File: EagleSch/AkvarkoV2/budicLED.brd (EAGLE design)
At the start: 114.3 x 160 mm, 75 parts, among them IC1 7805T, IC2 4051N, IC3 LF33CV, IC4 ESP01, J1 TRANSFLASH-LOCK, Q1 BD243C, Q2 BD243C, Q3 BD243C, Q4 BD243C, T1 2N5551, T2 2N5551, T3 2N5551, T4 2N5551, U1 ARDUINOR3-DIMENSION, X1 SMKDSP_1,5/2, X2 SMKDSP_1,5/8, X3 SMKDSP_1,5/3

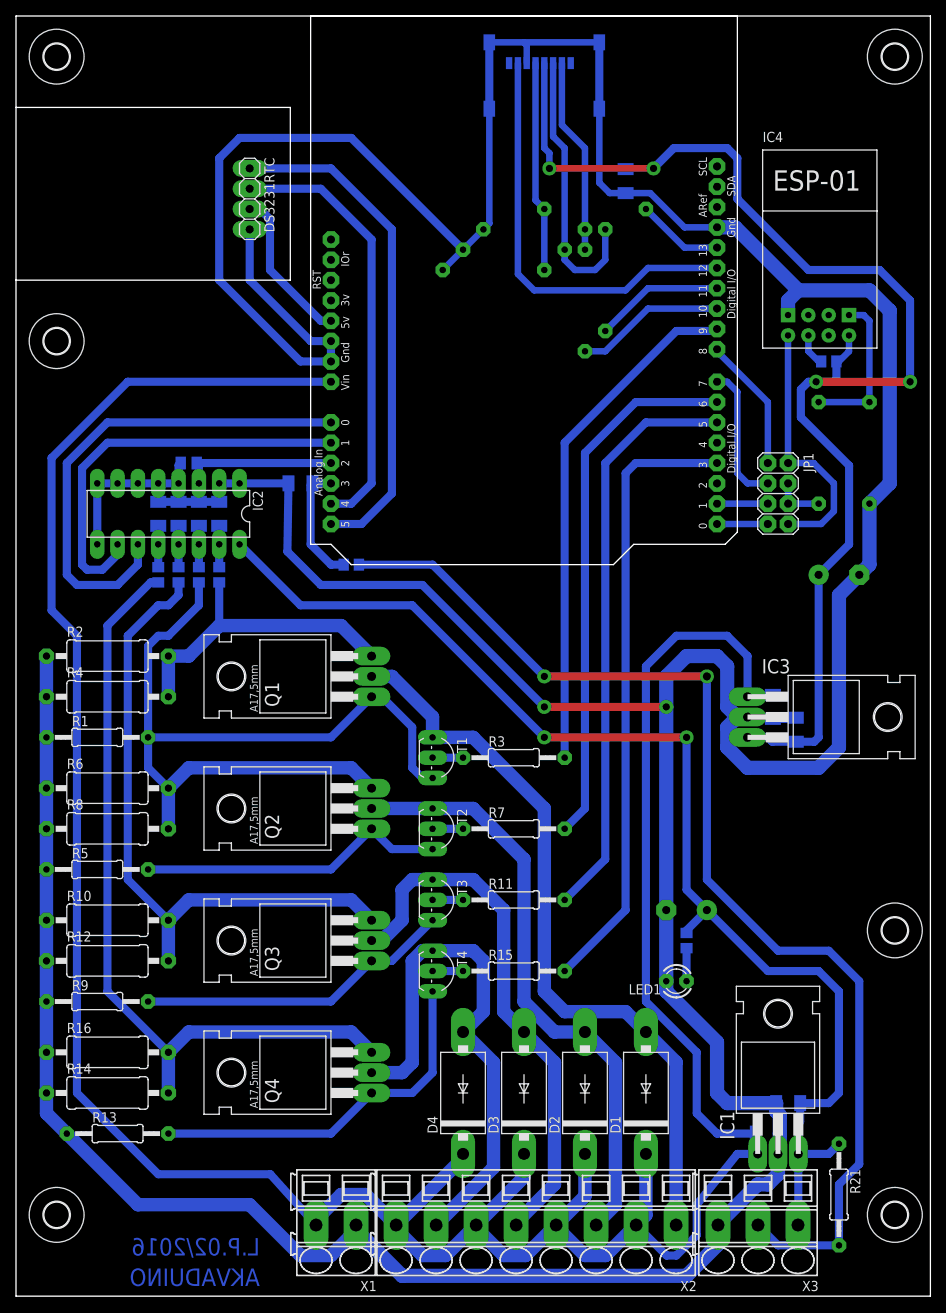
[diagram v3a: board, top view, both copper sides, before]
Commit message: DPS: - pridany LED, - dratove propojky nahrazeny reszistory 0R0, - doplnena rozlita med, - pridan zesilovaci prvek (tranzistor) k AD prevodnikum od snimani proudu ve vykonovem obvodu, - pridano nekolik filtracnich kapacit u napajeni IO.
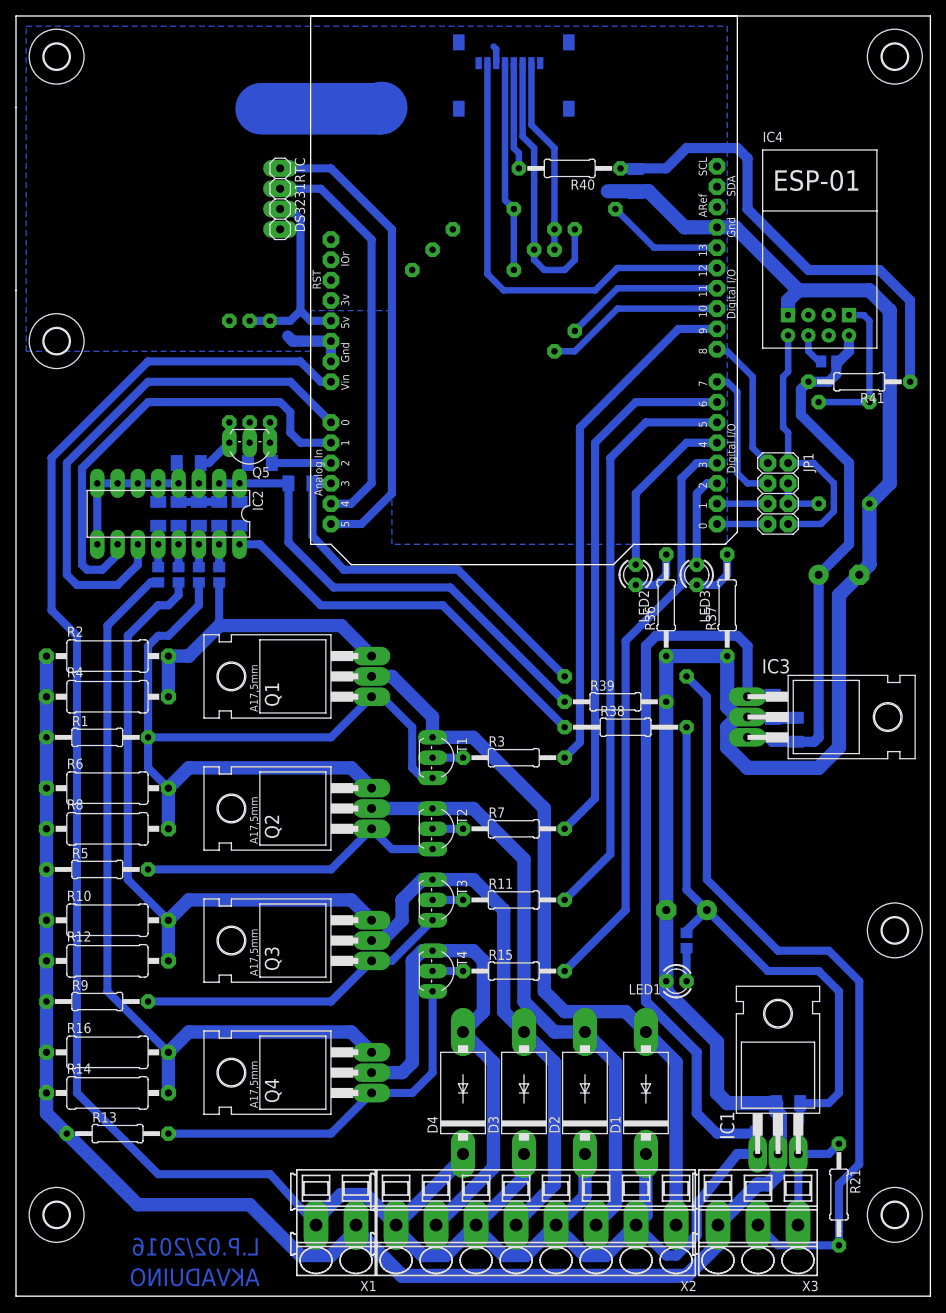
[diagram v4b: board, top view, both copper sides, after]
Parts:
- added C14, C15: 330n, rcl:C1206K
- added LED2, LED3: 2.2V 25mA, led:LED3MM
- added Q5: BC546A, transistor-npn:TO92-EBC
- added R33, R34, R35: 10k, rcl:0207/12
- added R36, R37: 390R, rcl:0207/12
- added R38: 0R0, rcl:0207/15
- added R39, R40, R41: 0R0, rcl:0207/12
- C11: device rcl:C0805K -> rcl:C1206K
- R17, R18, R19, R20: value 4k7 -> 1k
- R24: device rcl:R0805 -> rcl:0207/15
- moved R24 37.0 mm to (76.2, 77.5)
- moved J1 3.81 mm to (62.2, 153.7)
- moved DS3231RTC 3.81 mm to (33.0, 137.2)
- moved R25 3.81 mm to (68.6, 135.9)
- moved R27 3.81 mm to (69.8, 127.0)
- moved R29 3.81 mm to (67.3, 124.5)
- moved R26 3.81 mm to (55.9, 128.3)
- moved R28 3.81 mm to (58.4, 130.8)
- moved R30 3.81 mm to (61.0, 133.3)
- moved C13 1.27 mm to (77.5, 139.4)
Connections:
- new net GNDA: C1.2, C11.2, C12.2, C15.2, C2.2, C3.2, C4.2, IC2.1, IC2.2, IC2.4, IC2.5, IC2.6, IC2.7, IC2.8, IC2.9, R39.1
- new net LEDA: LED2.A, U1.D4
- new net LEDB: LED3.A, U1.D2
- new net N$40: C11.1, IC2.3, Q5.E
- new net N$43: LED2.K, R36.2
- new net N$44: DS3231RTC.3, R33.2, R34.1, U1.5V
- new net N$45: LED3.K, R37.2
- new net N$46: C15.1, IC2.16, R38.1
- new net N$47: J1.4, R40.2
- new net N$49: C13.1, R40.1, R41.1
- net +3V3: now also R41.2; no longer C13.1, J1.4
- net GND: now also R35.2, R36.1, R37.1, R39.2; no longer C1.2, C11.2, C12.2, C2.2, C3.2, C4.2, IC2.1, IC2.2, IC2.4, IC2.5, IC2.6, IC2.7, IC2.8, IC2.9
- net N$18: now also C14.1, Q5.C, R33.1; no longer C11.1, IC2.3
- net N$19: now also C14.2, Q5.B, R34.2, R35.1; no longer DS3231RTC.3, U1.5V
- net N$23: now also R38.2; no longer IC2.16
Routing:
- net GND: track 649.7 -> 412.9 mm, vias 2 -> 0
- net +3V3: track 164.2 -> 67.8 mm, vias 4 -> 0
- net GNDA: track 0.00 -> 93.6 mm
- net N$23: track 152.2 -> 87.6 mm, vias 2 -> 0
- net N$49: track 0.00 -> 59.1 mm
- net N$46: track 0.00 -> 52.4 mm
- net N$10: track 144.3 -> 96.0 mm, vias 2 -> 0
- net N$21: track 15.2 -> 47.8 mm
- net N$44: track 0.00 -> 25.7 mm
- net LEDA: track 0.00 -> 21.7 mm
- net N$19: track 19.7 -> 5.16 mm
- net N$47: track 0.00 -> 13.4 mm
- net LEDB: track 0.00 -> 12.0 mm
- net N$40: track 0.00 -> 7.27 mm
- net N$43: track 0.00 -> 6.88 mm
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- added copper zone on layer 16, net GND
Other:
- outline, holes or cut-outs redrawn

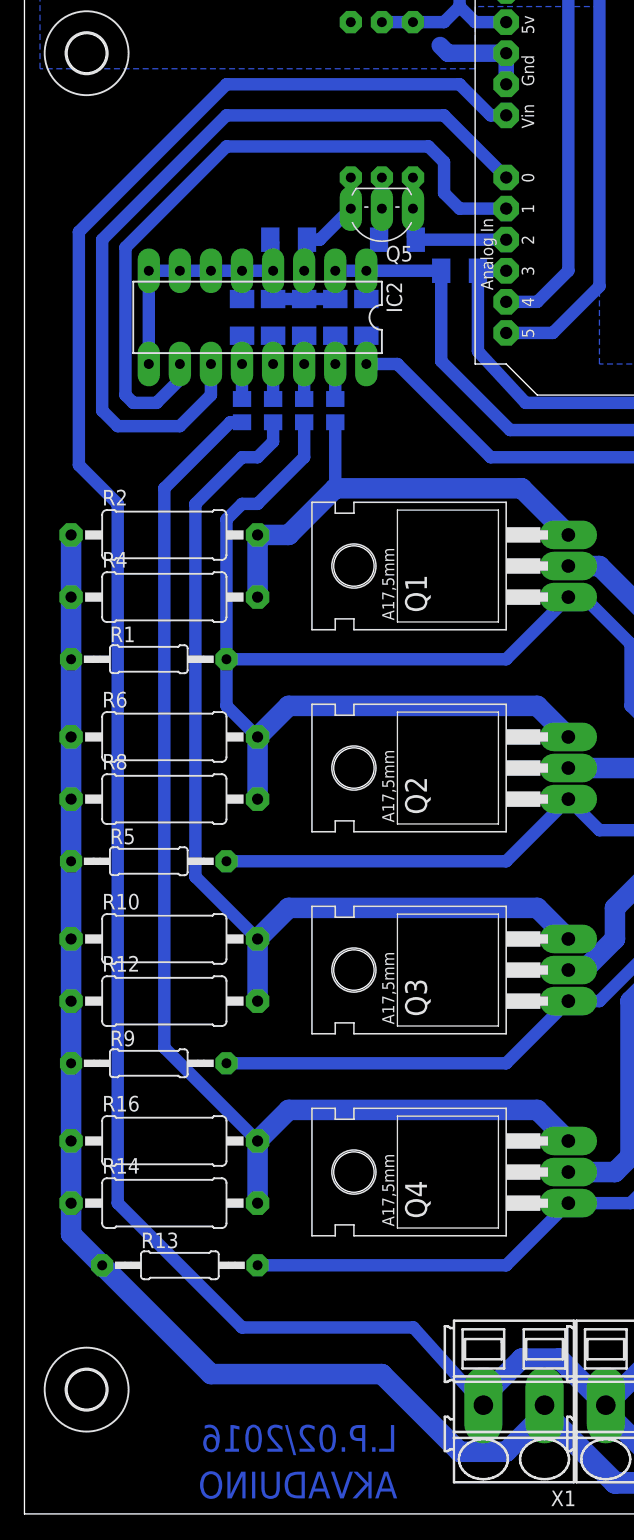
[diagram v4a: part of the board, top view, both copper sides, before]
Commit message: DPS: - posilena tloustka vykonove zeme a privodu napajeni k Arduino UNO
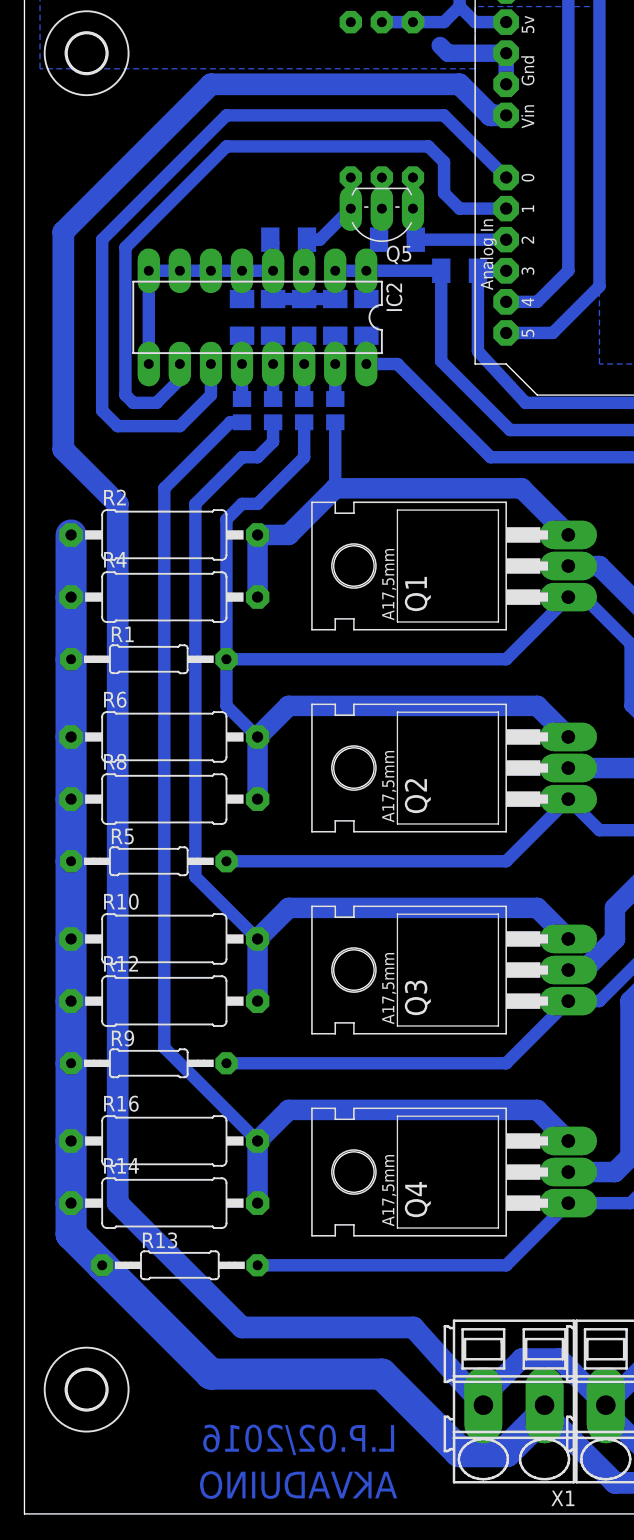
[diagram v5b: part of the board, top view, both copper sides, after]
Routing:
- net +12V: track 375.9 -> 377.7 mm
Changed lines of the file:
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@@
 <contactref element="X1" pad="1"/>
 <contactref element="X3" pad="3"/>
-<wire x1="3.81" y1="22.86" x2="3.81" y2="25.4" width="1.6764" layer="16"/>
-<wire x1="3.81" y1="25.4" x2="3.81" y2="30.48" width="1.6764" layer="16"/>
-<wire x1="3.81" y1="30.48" x2="3.81" y2="36.83" width="1.6764" layer="16"/>
-<wire x1="3.81" y1="36.83" x2="3.81" y2="41.91" width="1.6764" layer="16"/>
-<wire x1="3.81" y1="41.91" x2="3.81" y2="46.99" width="1.6764" layer="16"/>
-<wire x1="3.81" y1="46.99" x2="3.81" y2="53.34" width="1.6764" layer="16"/>
-<wire x1="3.81" y1="53.34" x2="3.81" y2="58.42" width="1.6764" layer="16"/>
-<wire x1="3.81" y1="58.42" x2="3.81" y2="63.5" width="1.6764" layer="16"/>
-<wire x1="3.81" y1="63.5" x2="3.81" y2="69.85" width="1.6764" layer="16"/>
-<wire x1="3.81" y1="69.85" x2="3.81" y2="74.93" width="1.6764" layer="16"/>
-<wire x1="3.81" y1="74.93" x2="3.81" y2="80.01" width="1.6764" layer="16"/>
+<wire x1="3.81" y1="22.86" x2="3.81" y2="25.4" width="2.54" layer="16"/>
+<wire x1="3.81" y1="25.4" x2="3.81" y2="30.48" width="2.54" layer="16"/>
+<wire x1="3.81" y1="30.48" x2="3.81" y2="36.83" width="2.54" layer="16"/>
+<wire x1="3.81" y1="36.83" x2="3.81" y2="41.91" width="2.54" layer="16"/>
+<wire x1="3.81" y1="41.91" x2="3.81" y2="46.99" width="2.54" layer="16"/>
+<wire x1="3.81" y1="46.99" x2="3.81" y2="53.34" width="2.54" layer="16"/>
+<wire x1="3.81" y1="53.34" x2="3.81" y2="58.42" width="2.54" layer="16"/>
+<wire x1="3.81" y1="58.42" x2="3.81" y2="63.5" width="2.54" layer="16"/>
+<wire x1="3.81" y1="63.5" x2="3.81" y2="69.85" width="2.54" layer="16"/>
+<wire x1="3.81" y1="69.85" x2="3.81" y2="74.93" width="2.54" layer="16"/>
+<wire x1="3.81" y1="74.93" x2="3.81" y2="80.01" width="2.54" layer="16"/>
 <wire x1="42.505" y1="8.89" x2="42.505" y2="8.295" width="1.016" layer="16"/>
 <wire x1="42.505" y1="8.295" x2="48.26" y2="2.54" width="1.778" layer="16"/>
@@
 <wire x1="87.63" y1="6.35" x2="87.63" y2="8.77" width="1.778" layer="16"/>
 <wire x1="87.63" y1="8.77" x2="87.75" y2="8.89" width="1.016" layer="16"/>
-<wire x1="6.35" y1="20.32" x2="15.24" y2="11.43" width="1.6764" layer="16"/>
-<wire x1="15.24" y1="11.43" x2="29.21" y2="11.43" width="1.6764" layer="16"/>
-<wire x1="29.21" y1="11.43" x2="35.56" y2="5.08" width="1.6764" layer="16"/>
-<wire x1="35.56" y1="5.08" x2="39.37" y2="5.08" width="1.6764" layer="16"/>
+<wire x1="6.35" y1="20.32" x2="15.24" y2="11.43" width="2.54" layer="16"/>
+<wire x1="15.24" y1="11.43" x2="29.21" y2="11.43" width="2.54" layer="16"/>
+<wire x1="29.21" y1="11.43" x2="35.56" y2="5.08" width="2.54" layer="16"/>
+<wire x1="35.56" y1="5.08" x2="39.37" y2="5.08" width="2.54" layer="16"/>
 <wire x1="87.75" y1="8.89" x2="87.75" y2="9.01" width="1.016" layer="16"/>
-<wire x1="6.35" y1="20.32" x2="3.81" y2="22.86" width="1.6764" layer="16"/>
+<wire x1="6.35" y1="20.32" x2="3.81" y2="22.86" width="2.54" layer="16"/>
 <wire x1="95.48" y1="20.32" x2="95.48" y2="18.01" width="1.778" layer="16"/>
 <wire x1="95.48" y1="18.01" x2="95.25" y2="17.78" width="1.016" layer="16"/>
@@
 <wire x1="81.28" y1="38.1" x2="81.28" y2="39.37" width="1.778" layer="16"/>
 <wire x1="42.505" y1="8.295" x2="42.505" y2="8.215" width="1.6764" layer="16"/>
-<wire x1="42.505" y1="8.215" x2="39.37" y2="5.08" width="1.6764" layer="16"/>
+<wire x1="42.505" y1="8.215" x2="39.37" y2="5.08" width="2.54" layer="16"/>
 <contactref element="J1" pad="6"/>
 <contactref element="J1" pad="S1"/>
@@
 <contactref element="X2" pad="8"/>
 <contactref element="X1" pad="2"/>
-<wire x1="16.51" y1="116.84" x2="4.445" y2="104.775" width="1.016" layer="16"/>
-<wire x1="4.445" y1="85.725" x2="7.62" y2="82.55" width="1.016" layer="16"/>
-<wire x1="7.62" y1="82.55" x2="7.62" y2="25.4" width="1.016" layer="16"/>
-<wire x1="7.62" y1="25.4" x2="17.78" y2="15.24" width="1.016" layer="16"/>
-<wire x1="17.78" y1="15.24" x2="31.79" y2="15.24" width="1.016" layer="16"/>
-<wire x1="31.79" y1="15.24" x2="37.505" y2="8.89" width="1.016" layer="16"/>
+<wire x1="15.24" y1="116.84" x2="3.175" y2="104.775" width="1.778" layer="16"/>
+<wire x1="3.175" y1="86.995" x2="7.62" y2="82.55" width="1.778" layer="16"/>
+<wire x1="7.62" y1="82.55" x2="7.62" y2="25.4" width="1.778" layer="16"/>
+<wire x1="7.62" y1="25.4" x2="17.78" y2="15.24" width="1.778" layer="16"/>
+<wire x1="17.78" y1="15.24" x2="31.79" y2="15.24" width="1.778" layer="16"/>
+<wire x1="31.79" y1="15.24" x2="37.505" y2="8.89" width="1.778" layer="16"/>
 <wire x1="47.51" y1="8.89" x2="47.51" y2="8.37" width="1.016" layer="16"/>
 <wire x1="50.8" y1="5.08" x2="53.7" y2="5.08" width="1.6764" layer="16"/>
@@
 <wire x1="55.88" y1="17.78" x2="55.88" y2="17.26" width="1.016" layer="16"/>
 <wire x1="55.88" y1="17.26" x2="47.51" y2="8.89" width="1.6764" layer="16"/>
-<wire x1="4.445" y1="104.775" x2="4.445" y2="85.725" width="1.016" layer="16"/>
+<wire x1="3.175" y1="104.775" x2="3.175" y2="86.995" width="1.778" layer="16"/>
 <wire x1="94.615" y1="75.16" x2="91.67" y2="75.16" width="1.27" layer="16"/>
 <wire x1="91.67" y1="75.16" x2="91.44" y2="74.93" width="1.27" layer="16"/>
-<wire x1="39.37" y1="114.3" x2="38.1" y2="114.3" width="1.016" layer="16"/>
-<wire x1="38.1" y1="114.3" x2="35.56" y2="116.84" width="1.016" layer="16"/>
-<wire x1="35.56" y1="116.84" x2="16.51" y2="116.84" width="1.016" layer="16"/>
+<wire x1="39.37" y1="114.3" x2="38.1" y2="114.3" width="1.778" layer="16"/>
+<wire x1="38.1" y1="114.3" x2="35.56" y2="116.84" width="1.778" layer="16"/>
+<wire x1="35.56" y1="116.84" x2="15.24" y2="116.84" width="1.778" layer="16"/>
 </signal>
 <signal name="N$21">
